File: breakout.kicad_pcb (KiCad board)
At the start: 2 copper layers, 12 x 20 mm, 6 parts

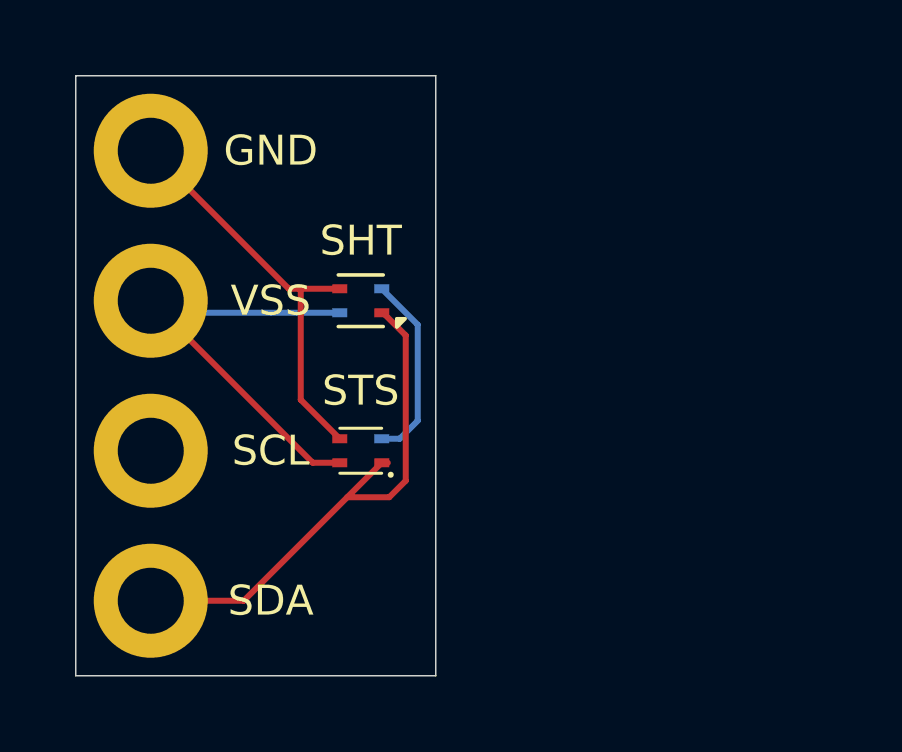
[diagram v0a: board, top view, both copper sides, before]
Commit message: make the breakouts separate but in one pcb
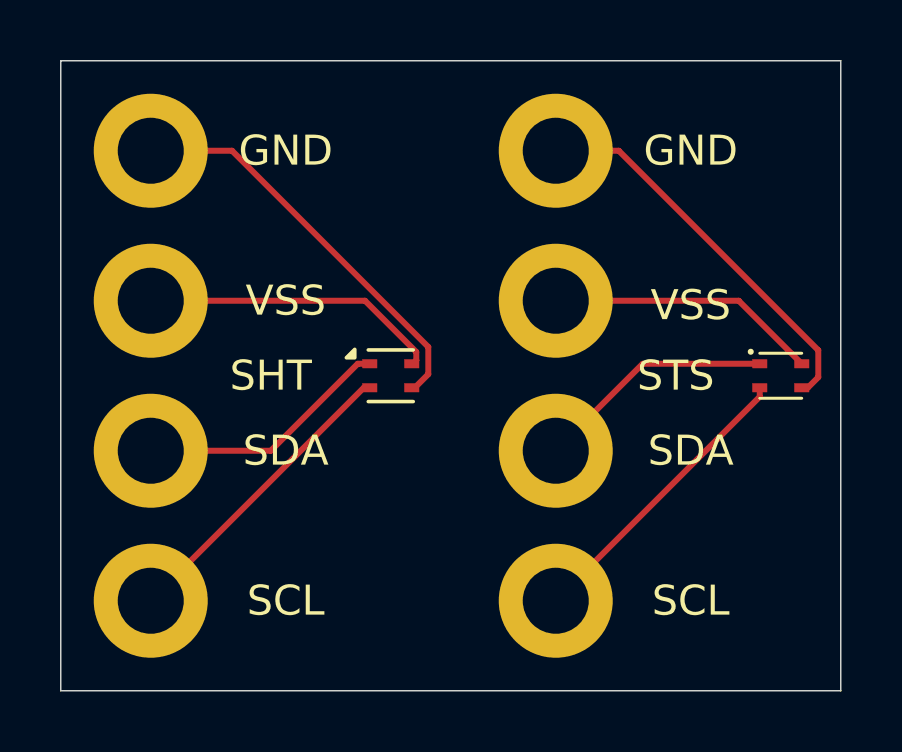
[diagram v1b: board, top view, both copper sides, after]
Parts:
- removed the SCL at (122.5, 92.5)
- removed the SDA at (122.5, 97.5)
- added GND: MountingHole_Pad, MountingHole:MountingHole_2.2mm_M2_DIN965_Pad, F.Cu at (136.0, 82.5)
- added SCL: MountingHole_Pad, MountingHole:MountingHole_2.2mm_M2_DIN965_Pad, F.Cu at (122.5, 97.5)
- added SCL: MountingHole_Pad, MountingHole:MountingHole_2.2mm_M2_DIN965_Pad, F.Cu at (136.0, 97.5)
- added SDA: MountingHole_Pad, MountingHole:MountingHole_2.2mm_M2_DIN965_Pad, F.Cu at (122.5, 92.5)
- added SDA: MountingHole_Pad, MountingHole:MountingHole_2.2mm_M2_DIN965_Pad, F.Cu at (136.0, 92.5)
- added VSS: MountingHole_Pad, MountingHole:MountingHole_2.2mm_M2_DIN965_Pad, F.Cu at (136.0, 87.5)
- moved STS 14.2 mm to (143.5, 90.0), turned to 0 degrees
- moved SHT 2.69 mm to (130.5, 90.0), turned to 0 degrees
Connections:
- GND pad 1: GND -> GND1
- SHT pad 3: GND -> GND1
- SHT pad 4: VSS -> VSS1
- STS pad 1: Net-(U1-SDA) -> Net-(U2-SDA)
- STS pad 2: Net-(U1-SCL) -> Net-(U2-SCL)
- VSS pad 1: VSS -> VSS1
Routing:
- net GND1: track 0.00 -> 13.6 mm
- net VSS1: track 0.00 -> 10.0 mm
- net Net-(U2-SCL): track 0.00 -> 9.92 mm
- net Net-(U1-SDA): track 17.9 -> 8.50 mm
- net Net-(U2-SDA): track 0.00 -> 8.00 mm
- net VSS: track 16.2 -> 9.07 mm
- net Net-(U1-SCL): track 6.34 -> 10.2 mm
- net GND: track 13.7 -> 13.1 mm
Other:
- board size 12 x 20 mm -> 26 x 21 mm
